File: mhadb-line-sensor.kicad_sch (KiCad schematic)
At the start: 114 parts, among them J1 Conn_01x04, J2 TC2030, J3 Conn_01x04_Pin, J4 Conn_01x04_Pin, SW1 SW_Push, SW2 SW_Push, SW3 SW_Push, SW4 SW_Push, U1 STM32F103C8Tx, U10 QRE1113GR, U11 QRE1113GR, U12 QRE1113GR, U13 HT753-1, U2 QRE1113GR, U3 SN65HVD230, U4 QRE1113GR, U5 QRE1113GR, U6 QRE1113GR, U7 QRE1113GR, U8 QRE1113GR, U9 QRE1113GR, Y1 8M

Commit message: schem: add missing footprints and ordering info
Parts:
- D10, D11, D12, D13, D14, D15, D16, D17, D18, D9: Basic (none) -> Z; JLCPCB Part # (none) -> C2874885; Manufacturer (none) -> Worldsemi; Manufacturer Part Number (none) -> WS2812B-V5/W; now left out of the parts list
- J1: footprint (none) -> Connector_JST:JST_PH_S4B-PH-K_1x04_P2.00mm_Horizontal; Basic (none) -> Z; JLCPCB Part # (none) -> C157926; Manufacturer (none) -> JST; Manufacturer Part Number (none) -> S4B-PH-K-S(LF)(SN); now left out of the parts list
- U1: Basic (none) -> E; JLCPCB Part # (none) -> C8734; Manufacturer (none) -> STMicroelectronics; Manufacturer Part Number (none) -> STM32F103C8T6

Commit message: schem: add title
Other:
- company: (none) -> Mechadiabatik
- title: (none) -> MHADB Line sensor
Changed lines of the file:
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@@
 	(generator_version "9.0")
 	(paper "A4")
+	(title_block
+		(title "MHADB Line sensor")
+		(date "2026-01-09")
+		(rev "01")
+		(company "Mechadiabatik")
+	)
 	(rectangle
 		(start 16.51 13.97)

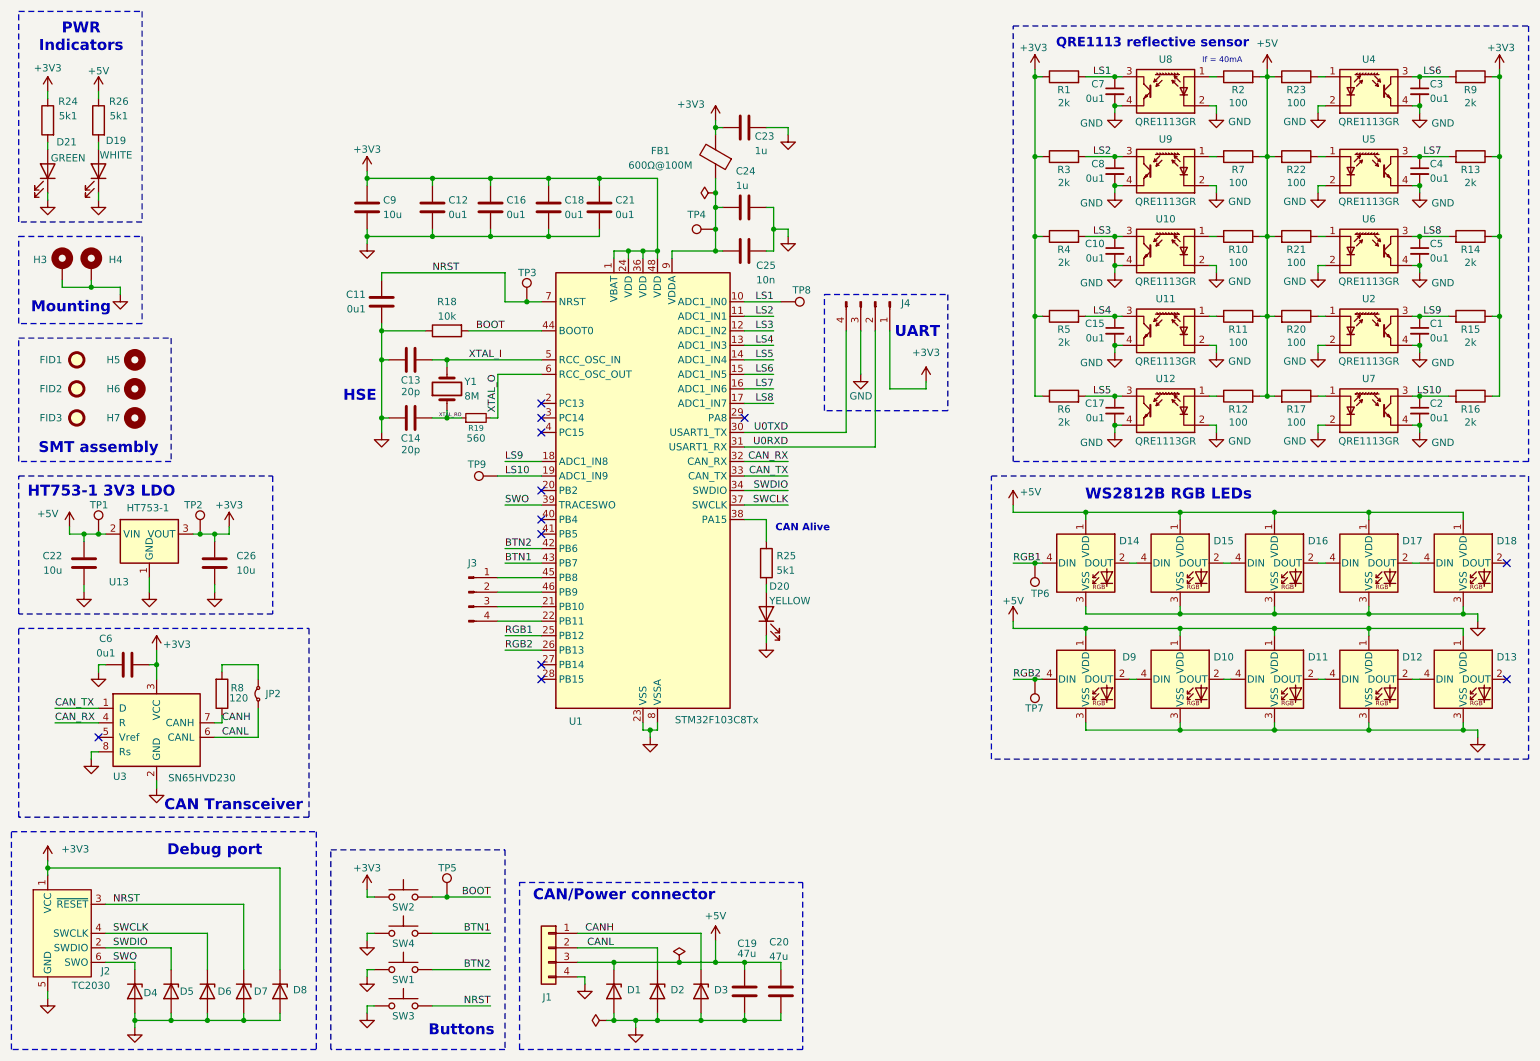
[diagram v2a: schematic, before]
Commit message: schem: renumber
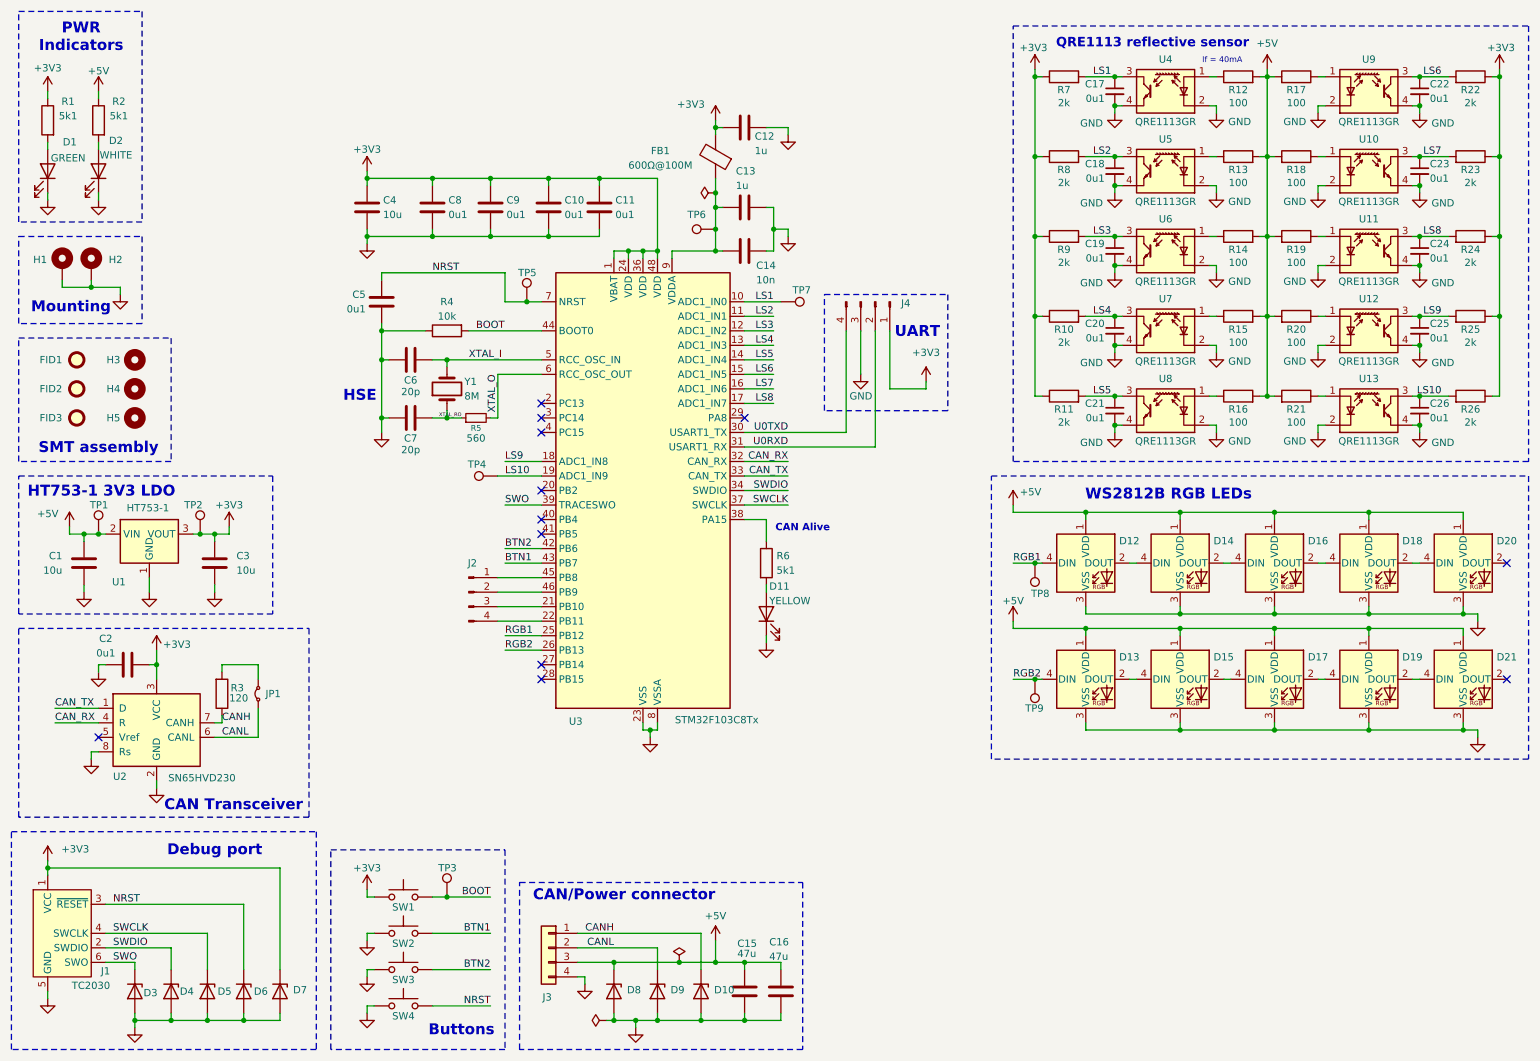
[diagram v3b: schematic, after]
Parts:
- renumbered C22 to C1, C18 to C10, C21 to C11, C23 to C12, C24 to C13, C25 to C14, C19 to C15, C20 to C16, C7 to C17, C8 to C18, C10 to C19, C6 to C2, C15 to C20, C17 to C21, C3 to C22, C4 to C23, C5 to C24, C1 to C25, C2 to C26, C26 to C3, C9 to C4, C11 to C5, C13 to C6, C14 to C7, C12 to C8, C16 to C9, D21 to D1, D3 to D10, D20 to D11, D14 to D12, D9 to D13, D15 to D14, D10 to D15, D11 to D17, D17 to D18, D12 to D19, D19 to D2, D18 to D20, D13 to D21, D4 to D3, D5 to D4, D6 to D5, D7 to D6, D8 to D7, D1 to D8, D2 to D9, H3 to H1, H4 to H2, H5 to H3, H6 to H4, H7 to H5, J2 to J1, J3 to J2, J1 to J3, JP2 to JP1, R24 to R1, R5 to R10, R6 to R11, R2 to R12, R7 to R13, R10 to R14, R11 to R15, R12 to R16, R23 to R17, R22 to R18, R21 to R19, R26 to R2, R17 to R21, R9 to R22, R13 to R23, R14 to R24, R15 to R25, R16 to R26, R8 to R3, R18 to R4, R19 to R5, R25 to R6, R1 to R7, R3 to R8, R4 to R9, SW2 to SW1, SW4 to SW2, SW1 to SW3, SW3 to SW4, TP5 to TP3, TP9 to TP4, TP3 to TP5, TP4 to TP6, TP8 to TP7, TP6 to TP8, TP7 to TP9, U13 to U1, U5 to U10, U6 to U11, U2 to U12, U7 to U13, U3 to U2, U1 to U3, U8 to U4, U9 to U5, U10 to U6, U11 to U7, U12 to U8, U4 to U9

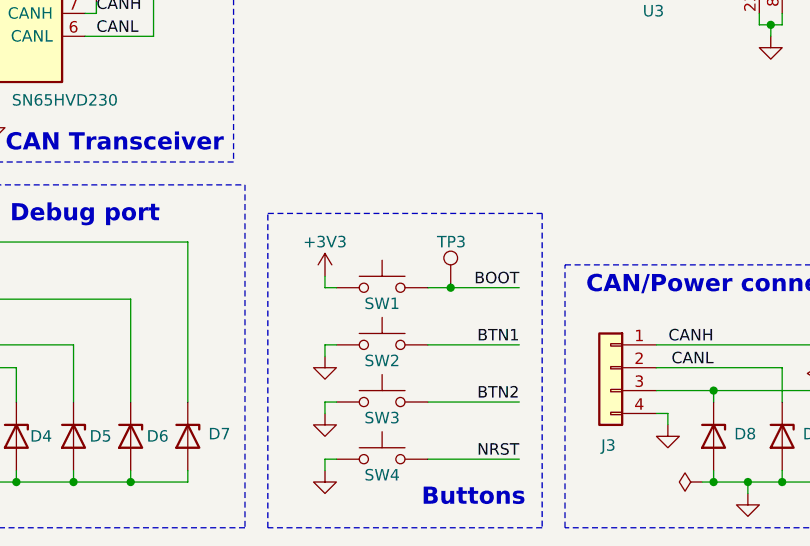
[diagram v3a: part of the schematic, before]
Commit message: schem/pcb: add EM stop btn
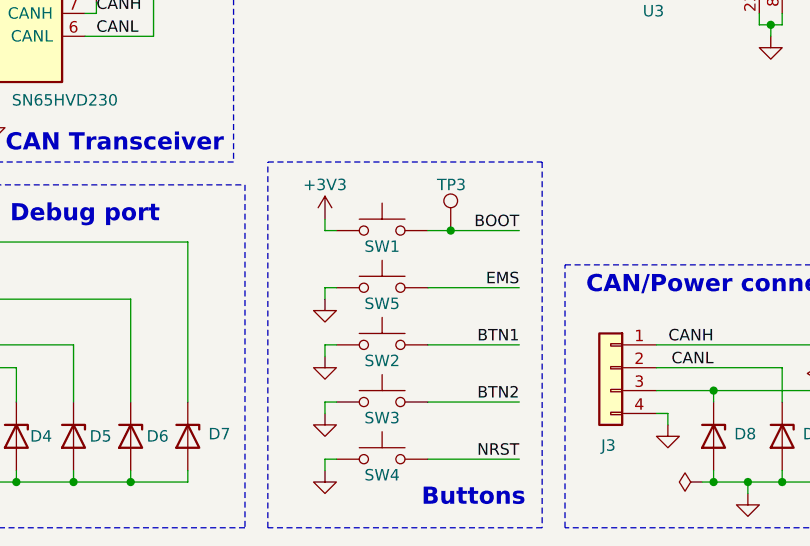
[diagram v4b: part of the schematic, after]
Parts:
- added SW5: SW_Push, Button_Switch_THT:SW_SPST_Omron_B3F-40xx, symbol Switch:SW_Push
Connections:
- net GND: now also SW5.1
- new net EMS: SW5.2
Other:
- moved on the sheet: SW1, TP3
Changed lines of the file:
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@@
 	)
 	(rectangle
-		(start 71.12 160.655)
+		(start 71.12 154.94)
 		(end 101.6 195.58)
 		(stroke
@@
 	)
 	(junction
-		(at 91.44 168.91)
+		(at 91.44 162.56)
 		(diameter 0)
 		(color 0 0 0 0)
@@
 	(wire
 		(pts
+			(xy 77.47 168.91) (xy 78.74 168.91)
+		)
+		(stroke
+			(width 0)
+			(type default)
+		)
+	)
+	(wire
+		(pts
 			(xy 219.71 101.6) (xy 236.22 101.6)
 		)
@@
 	(wire
 		(pts
+			(xy 88.9 168.91) (xy 99.06 168.91)
+		)
+		(stroke
+			(width 0)
+			(type default)
+		)
+	)
+	(wire
+		(pts
 			(xy 40.64 128.27) (xy 40.64 130.81)
 		)
@@
 	(wire
 		(pts
-			(xy 78.74 168.91) (xy 77.47 168.91)
+			(xy 78.74 162.56) (xy 77.47 162.56)
 		)
 		(stroke
@@
 	(wire
 		(pts
-			(xy 77.47 168.91) (xy 77.47 167.64)
+			(xy 77.47 162.56) (xy 77.47 161.29)
 		)
 		(stroke
@@
 	(wire
 		(pts
-			(xy 88.9 168.91) (xy 91.44 168.91)
+			(xy 88.9 162.56) (xy 91.44 162.56)
 		)
 		(stroke
@@
 	(wire
 		(pts
-			(xy 91.44 168.91) (xy 99.06 168.91)
+			(xy 91.44 162.56) (xy 99.06 162.56)
 		)
 		(stroke
@@
 	(wire
 		(pts
+			(xy 77.47 170.18) (xy 77.47 168.91)
+		)
+		(stroke
+			(width 0)
+			(type default)
+		)
+	)
+	(wire
+		(pts
 			(xy 88.9 187.96) (xy 99.06 187.96)
 		)
@@
 	)
 	(label "BOOT"
-		(at 99.06 168.91 180)
+		(at 99.06 162.56 180)
 		(effects
 			(font
@@
 		)
 	)
+	(label "EMS"
+		(at 99.06 168.91 180)
+		(effects
+			(font
+				(size 1.27 1.27)
+			)
+			(justify right bottom)
+		)
+	)
 	(label "SWO"
 		(at 101.6 100.33 0)
@@
 	)
 	(symbol
+		(lib_id "Switch:SW_Push")
+		(at 83.82 168.91 0)
+		(unit 1)
+		(exclude_from_sim no)
+		(in_bom no)
+		(on_board yes)
+		(dnp no)
+		(property "Reference" "SW5"
+			(at 83.82 170.688 0)
+			(effects
+				(font
+					(size 1.27 1.27)
+				)
+			)
+		)
+		(property "Value" "SW_Push"
+			(at 83.82 163.83 0)
+			(effects
+				(font
+					(size 1.27 1.27)
+				)
+				(hide yes)
+			)
+		)
+		(property "Footprint" "Button_Switch_THT:SW_SPST_Omron_B3F-40xx"
+			(at 83.82 163.83 0)
+			(effects
+				(font
+					(size 1.27 1.27)
+				)
+				(hide yes)
+			)
+		)
+		(property "Datasheet" "~"
+			(at 83.82 163.83 0)
+			(effects
+				(font
+					(size 1.27 1.27)
+				)
+				(hide yes)
+			)
+		)
+		(property "Description" "Push button switch, generic, two pins"
+			(at 83.82 168.91 0)
+			(effects
+				(font
+					(size 1.27 1.27)
+				)
+				(hide yes)
+			)
+		)
+		(property "Manufacturer" "OMRON"
+			(at 83.82 168.91 0)
+			(effects
+				(font
+					(size 1.27 1.27)
+				)
+				(hide yes)
+			)
+		)
+		(property "Manufacturer Part Number" "B3F-4055"
+			(at 83.82 168.91 0)
+			(effects
+				(font
+					(size 1.27 1.27)
+				)
+				(hide yes)
+			)
+		)
+		(property "Basic" "Z"
+			(at 83.82 168.91 0)
+			(effects
+				(font
+					(size 1.27 1.27)
+				)
+				(hide yes)
+			)
+		)
+		(property "JLCPCB Part #" "C84931"
+			(at 83.82 168.91 0)
+			(effects
+				(font
+					(size 1.27 1.27)
+				)
+				(hide yes)
+			)
+		)
+		(pin "2"
+		)
+		(pin "1"
+		)
+		(instances
+			(project "mhadb-line-sensor"
+				(path "/dc023b14-f8af-47bb-9afb-84a8ab4a9288"
+					(reference "SW5")
+					(unit 1)
+				)
+			)
+		)
+	)
+	(symbol
 		(lib_id "Device:R")
 		(at 240.03 67.31 270)
@@
 	(symbol
 		(lib_id "Switch:SW_Push")
-		(at 83.82 168.91 0)
+		(at 83.82 162.56 0)
 		(unit 1)
 		(exclude_from_sim no)
@@
 		(dnp no)
 		(property "Reference" "SW1"
-			(at 83.82 170.688 0)
+			(at 83.82 164.338 0)
 			(effects
 				(font
@@
 		)
 		(property "Value" "SW_Push"
-			(at 83.82 163.83 0)
+			(at 83.82 157.48 0)
 			(effects
 				(font
@@
 		)
 		(property "Footprint" "Button_Switch_SMD:SW_SPST_TS-1088-xR020"
-			(at 83.82 163.83 0)
+			(at 83.82 157.48 0)
 			(effects
 				(font
@@
 		)
 		(property "Datasheet" "~"
-			(at 83.82 163.83 0)
+			(at 83.82 157.48 0)
 			(effects
 				(font
@@
 		)
 		(property "Description" "Push button switch, generic, two pins"
-			(at 83.82 168.91 0)
+			(at 83.82 162.56 0)
 			(effects
 				(font
@@
 		)
 		(property "Manufacturer" "XUNPU"
-			(at 83.82 168.91 0)
+			(at 83.82 162.56 0)
 			(effects
 				(font
@@
 		)
 		(property "Manufacturer Part Number" "TS-1088-AR02016"
-			(at 83.82 168.91 0)
+			(at 83.82 162.56 0)
 			(effects
 				(font
@@
 		)
 		(property "Basic" "Y"
-			(at 83.82 168.91 0)
+			(at 83.82 162.56 0)
 			(effects
 				(font
@@
 		)
 		(property "JLCPCB Part #" "C720477"
-			(at 83.82 168.91 0)
+			(at 83.82 162.56 0)
 			(effects
 				(font
@@
 	(symbol
 		(lib_id "power:+3V3")
-		(at 77.47 167.64 0)
+		(at 77.47 161.29 0)
 		(unit 1)
 		(exclude_from_sim no)
@@
 		(dnp no)
 		(property "Reference" "#PWR020"
-			(at 77.47 171.45 0)
+			(at 77.47 165.1 0)
 			(effects
 				(font
@@
 		)
 		(property "Value" "+3V3"
-			(at 77.47 163.83 0)
+			(at 77.47 157.48 0)
 			(effects
 				(font
@@
 		)
 		(property "Footprint" ""
-			(at 77.47 167.64 0)
+			(at 77.47 161.29 0)
 			(effects
 				(font
@@
 		)
 		(property "Datasheet" ""
-			(at 77.47 167.64 0)
+			(at 77.47 161.29 0)
 			(effects
 				(font
@@
 		)
 		(property "Description" "Power symbol creates a global label with name \"+3V3\""
-			(at 77.47 167.64 0)
+			(at 77.47 161.29 0)
 			(effects
 				(font
@@
 	(symbol
 		(lib_id "power:GND")
+		(at 77.47 170.18 0)
+		(unit 1)
+		(exclude_from_sim no)
+		(in_bom yes)
+		(on_board yes)
+		(dnp no)
+		(property "Reference" "#PWR062"
+			(at 77.47 176.53 0)
+			(effects
+				(font
+					(size 1.27 1.27)
+				)
+				(hide yes)
+			)
+		)
+		(property "Value" "GND"
+			(at 77.216 174.498 0)
+			(effects
+				(font
+					(size 1.27 1.27)
+				)
+				(hide yes)
+			)
+		)
+		(property "Footprint" ""
+			(at 77.47 170.18 0)
+			(effects
+				(font
+					(size 1.27 1.27)
+				)
+				(hide yes)
+			)
+		)
+		(property "Datasheet" ""
+			(at 77.47 170.18 0)
+			(effects
+				(font
+					(size 1.27 1.27)
+				)
+				(hide yes)
+			)
+		)
+		(property "Description" "Power symbol creates a global label with name \"GND\" , ground"
+			(at 77.47 170.18 0)
+			(effects
+				(font
+					(size 1.27 1.27)
+				)
+				(hide yes)
+			)
+		)
+		(pin "1"
+		)
+		(instances
+			(project "mhadb-line-sensor"
+				(path "/dc023b14-f8af-47bb-9afb-84a8ab4a9288"
+					(reference "#PWR062")
+					(unit 1)
+				)
+			)
+		)
+	)
+	(symbol
+		(lib_id "power:GND")
 		(at 151.13 53.34 0)
 		(unit 1)
@@
 	(symbol
 		(lib_id "Connector:TestPoint")
-		(at 91.44 168.91 0)
+		(at 91.44 162.56 0)
 		(unit 1)
 		(exclude_from_sim no)
@@
 		(dnp no)
 		(property "Reference" "TP3"
-			(at 89.916 163.83 0)
+			(at 89.916 157.48 0)
 			(effects
 				(font
@@
 		)
 		(property "Value" "TestPoint"
-			(at 93.98 166.8779 0)
+			(at 93.98 160.5279 0)
 			(effects
 				(font
@@
 		)
 		(property "Footprint" "TestPoint:TestPoint_Pad_D2.0mm"
-			(at 96.52 168.91 0)
+			(at 96.52 162.56 0)
 			(effects
 				(font
@@
 		)
 		(property "Datasheet" "~"
-			(at 96.52 168.91 0)
+			(at 96.52 162.56 0)
 			(effects
 				(font
@@
 		)
 		(property "Description" "test point"
-			(at 91.44 168.91 0)
+			(at 91.44 162.56 0)
 			(effects
 				(font

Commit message: pcb: initial rough layout
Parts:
- removed SW5: SW_Push, Button_Switch_THT:SW_SPST_Omron_B3F-40xx, symbol Switch:SW_Push
- removed TP3, TP5, TP6: TestPoint, TestPoint:TestPoint_Pad_D2.0mm, symbol Connector:TestPoint
- D12, D13, D14, D15, D16, D17, D18, D19, D20, D21, J3: now in the parts list
- R12, R13, R14, R15, R16, R17, R18, R19, R20, R21: footprint Capacitor_SMD:C_1206_3216Metric -> Resistor_SMD:R_1206_3216Metric
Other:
- moved on the sheet: SW1

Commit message: schem/pcb: add BOOT1 strapping
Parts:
- added JP2: Jumper_2_Small_Bridged, Jumper:SolderJumper-2_P1.3mm_Bridged_RoundedPad1.0x1.5mm, symbol Jumper:Jumper_2_Small_Bridged
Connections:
- net GND: now also JP2.1 (A)
- net at U3.20 (PB2): now also JP2.2 (B)
- no-connect marks 12 -> 11
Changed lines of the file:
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@@
 		(at 107.95 128.27)
 	)
-	(no_connect
-		(at 107.95 97.79)
-	)
 	(wire
 		(pts
@@
 	(wire
 		(pts
+			(xy 96.52 97.79) (xy 96.52 100.33)
+		)
+		(stroke
+			(width 0)
+			(type default)
+		)
+	)
+	(wire
+		(pts
 			(xy 194.31 81.28) (xy 195.58 81.28)
 		)
@@
 	(wire
 		(pts
+			(xy 102.87 97.79) (xy 96.52 97.79)
+		)
+		(stroke
+			(width 0)
+			(type default)
+		)
+	)
+	(wire
+		(pts
 			(xy 219.71 121.92) (xy 236.22 121.92)
 		)
@@
 	)
 	(symbol
+		(lib_id "power:GND")
+		(at 96.52 100.33 0)
+		(unit 1)
+		(exclude_from_sim no)
+		(in_bom yes)
+		(on_board yes)
+		(dnp no)
+		(fields_autoplaced yes)
+		(property "Reference" "#PWR062"
+			(at 96.52 106.68 0)
+			(effects
+				(font
+					(size 1.27 1.27)
+				)
+				(hide yes)
+			)
+		)
+		(property "Value" "GND"
+			(at 96.52 105.41 0)
+			(effects
+				(font
+					(size 1.27 1.27)
+				)
+				(hide yes)
+			)
+		)
+		(property "Footprint" ""
+			(at 96.52 100.33 0)
+			(effects
+				(font
+					(size 1.27 1.27)
+				)
+				(hide yes)
+			)
+		)
+		(property "Datasheet" ""
+			(at 96.52 100.33 0)
+			(effects
+				(font
+					(size 1.27 1.27)
+				)
+				(hide yes)
+			)
+		)
+		(property "Description" "Power symbol creates a global label with name \"GND\" , ground"
+			(at 96.52 100.33 0)
+			(effects
+				(font
+					(size 1.27 1.27)
+				)
+				(hide yes)
+			)
+		)
+		(pin "1"
+		)
+		(instances
+			(project "mhadb-line-sensor"
+				(path "/dc023b14-f8af-47bb-9afb-84a8ab4a9288"
+					(reference "#PWR062")
+					(unit 1)
+				)
+			)
+		)
+	)
+	(symbol
 		(lib_id "Connector:Conn_ARM_SWD_TagConnect_TC2030-NL")
 		(at 24.13 175.26 0)
@@
 					(unit 1)
 				)
+			)
+		)
+	)
+	(symbol
+		(lib_id "Jumper:Jumper_2_Small_Bridged")
+		(at 105.41 97.79 0)
+		(unit 1)
+		(exclude_from_sim no)
+		(in_bom yes)
+		(on_board yes)
+		(dnp no)
+		(property "Reference" "JP2"
+			(at 102.362 96.52 0)
+			(effects
+				(font
+					(size 1.27 1.27)
+				)
+			)
+		)
+		(property "Value" "Jumper_2_Small_Bridged"
+			(at 105.41 95.25 0)
+			(effects
+				(font
+					(size 1.27 1.27)
+				)
+				(hide yes)
+			)
+		)
+		(property "Footprint" "Jumper:SolderJumper-2_P1.3mm_Bridged_RoundedPad1.0x1.5mm"
+			(at 105.41 97.79 0)
+			(effects
+				(font
+					(size 1.27 1.27)
+				)
+				(hide yes)
+			)
+		)
+		(property "Datasheet" "~"
+			(at 105.41 97.79 0)
+			(effects
+				(font
+					(size 1.27 1.27)
+				)
+				(hide yes)
+			)
+		)
+		(property "Description" "Jumper, 2-pole, small symbol, bridged"
+			(at 105.41 97.79 0)
+			(effects
+				(font
+					(size 1.27 1.27)
+				)
+				(hide yes)
+			)
+		)
+		(pin "2"
+		)
+		(pin "1"
+		)
+		(instances
+			(project ""
+				(path "/dc023b14-f8af-47bb-9afb-84a8ab4a9288"
+					(reference "JP2")
+					(unit 1)
+				)
